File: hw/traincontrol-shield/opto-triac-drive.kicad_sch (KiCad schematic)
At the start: 6 parts, among them U5 MOC3021M, U6 MOC3021M

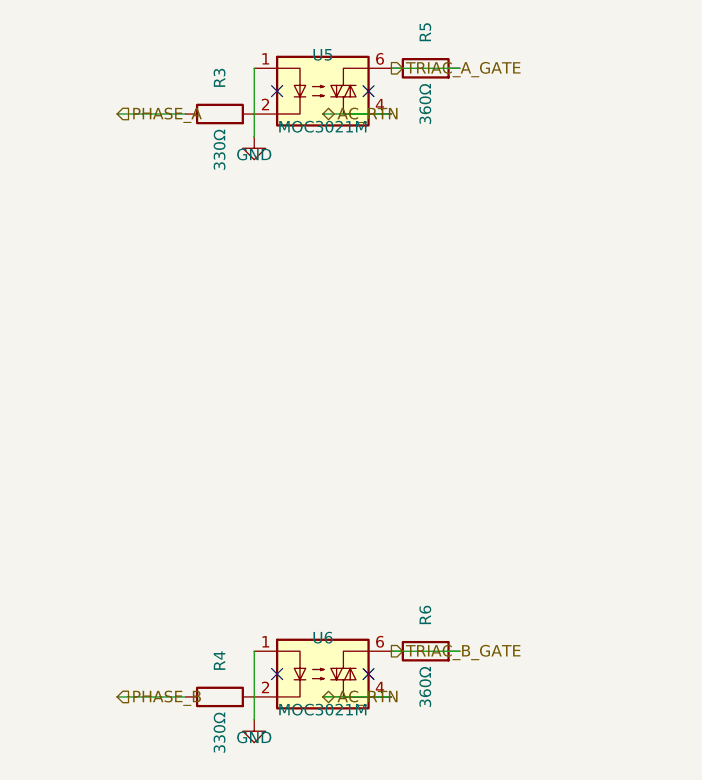
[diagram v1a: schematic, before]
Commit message: Fix hierarchical label placement and orientation in sub-sheets
Root cause: hlabel() placed the label at lx (stub tip) instead of x
(circuit connection point), mirroring the Issue-2 glabel bug fixed in
commit 2270223.

Fix applied to hlabel():
  (at {lx} ...) → (at {x} ...)  — label now sits at the circuit endpoint

Angle convention (matches label body direction):
  angle=180 → body extends LEFT  — left-side input/bidirectional labels
  angle=0   → body extends RIGHT — right-side output/bidirectional labels

Sheets affected: zero-crossing, xor-interlock, opto-triac-drive,
rail-voltage-sense; triacs-snubbers and mcu already had correct angles.

Co-Authored-By: Claude Sonnet 4.6 <noreply@anthropic.com>
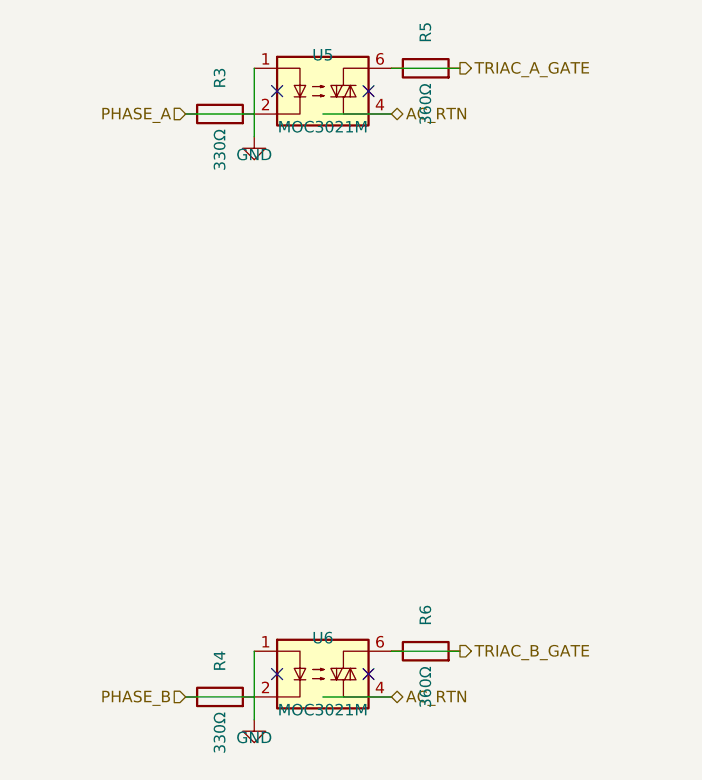
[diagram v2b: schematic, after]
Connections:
- net PHASE_A: now also R3.2, U5.2
- net PHASE_B: now also R4.2, U6.2
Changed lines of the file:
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@@
 	(hierarchical_label "AC_RTN"
 		(shape bidirectional)
-		(at 80.01 92.71000000000001 0)
+		(at 87.63000000000001 92.71000000000001 0)
 		(fields_autoplaced yes)
 		(effects (font (size 1.27 1.27)) (justify left bottom))
 		(property "Intersheetrefs" "${INTERSHEET_REFS}"
-			(at 80.01 92.71000000000001 0)
+			(at 87.63000000000001 92.71000000000001 0)
 			(effects (font (size 1.27 1.27)) (hide yes))
 		)
@@
 	)
 	(wire
-		(pts (xy 57.15 92.71000000000001) (xy 64.77 92.71000000000001))
+		(pts (xy 64.77 92.71000000000001) (xy 72.39 92.71000000000001))
 		(stroke (width 0) (type solid))
 	)
 	(hierarchical_label "PHASE_A"
 		(shape input)
-		(at 57.15 92.71000000000001 0)
-		(fields_autoplaced yes)
-		(effects (font (size 1.27 1.27)) (justify left bottom))
-		(property "Intersheetrefs" "${INTERSHEET_REFS}"
-			(at 57.15 92.71000000000001 0)
+		(at 64.77 92.71000000000001 180)
+		(fields_autoplaced yes)
+		(effects (font (size 1.27 1.27)) (justify right bottom))
+		(property "Intersheetrefs" "${INTERSHEET_REFS}"
+			(at 64.77 92.71000000000001 0)
 			(effects (font (size 1.27 1.27)) (hide yes))
 		)
@@
 	(hierarchical_label "TRIAC_A_GATE"
 		(shape output)
-		(at 87.63000000000001 87.63 0)
+		(at 95.25000000000001 87.63 0)
 		(fields_autoplaced yes)
 		(effects (font (size 1.27 1.27)) (justify left bottom))
 		(property "Intersheetrefs" "${INTERSHEET_REFS}"
-			(at 87.63000000000001 87.63 0)
+			(at 95.25000000000001 87.63 0)
 			(effects (font (size 1.27 1.27)) (hide yes))
 		)
@@
 	(hierarchical_label "AC_RTN"
 		(shape bidirectional)
-		(at 80.01 157.48 0)
+		(at 87.63000000000001 157.48 0)
 		(fields_autoplaced yes)
 		(effects (font (size 1.27 1.27)) (justify left bottom))
 		(property "Intersheetrefs" "${INTERSHEET_REFS}"
-			(at 80.01 157.48 0)
+			(at 87.63000000000001 157.48 0)
 			(effects (font (size 1.27 1.27)) (hide yes))
 		)
@@
 	)
 	(wire
-		(pts (xy 57.15 157.48) (xy 64.77 157.48))
+		(pts (xy 64.77 157.48) (xy 72.39 157.48))
 		(stroke (width 0) (type solid))
 	)
 	(hierarchical_label "PHASE_B"
 		(shape input)
-		(at 57.15 157.48 0)
-		(fields_autoplaced yes)
-		(effects (font (size 1.27 1.27)) (justify left bottom))
-		(property "Intersheetrefs" "${INTERSHEET_REFS}"
-			(at 57.15 157.48 0)
+		(at 64.77 157.48 180)
+		(fields_autoplaced yes)
+		(effects (font (size 1.27 1.27)) (justify right bottom))
+		(property "Intersheetrefs" "${INTERSHEET_REFS}"
+			(at 64.77 157.48 0)
 			(effects (font (size 1.27 1.27)) (hide yes))
 		)
@@
 	(hierarchical_label "TRIAC_B_GATE"
 		(shape output)
-		(at 87.63000000000001 152.4 0)
+		(at 95.25000000000001 152.4 0)
 		(fields_autoplaced yes)
 		(effects (font (size 1.27 1.27)) (justify left bottom))
 		(property "Intersheetrefs" "${INTERSHEET_REFS}"
-			(at 87.63000000000001 152.4 0)
-			(effects (font (size 1.27 1.27)) (hide yes))
-		)
+			(at 95.25000000000001 152.4 0)
+			(effects (font (size 1.27 1.27)) (hide yes))
+		)

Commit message: Fix stub wire short-circuit across R3/R5 in opto-triac sheet
With the label placed at x (circuit pin), the STUB wire from x to lx
was spanning the entire resistor body — creating a direct short across
both the LED series resistor (R3/R4) and the gate resistor (R5/R6).

Fix: shift x outward by one STUB so the stub wire terminates at the
resistor's outer pin rather than running across it:
  phase label:  x = cx-7.62-3.81-3.81-STUB  (lx lands on R pin2)
  gate  label:  x = gx+3.81+STUB             (lx lands on R gate pin1)

Co-Authored-By: Claude Sonnet 4.6 <noreply@anthropic.com>
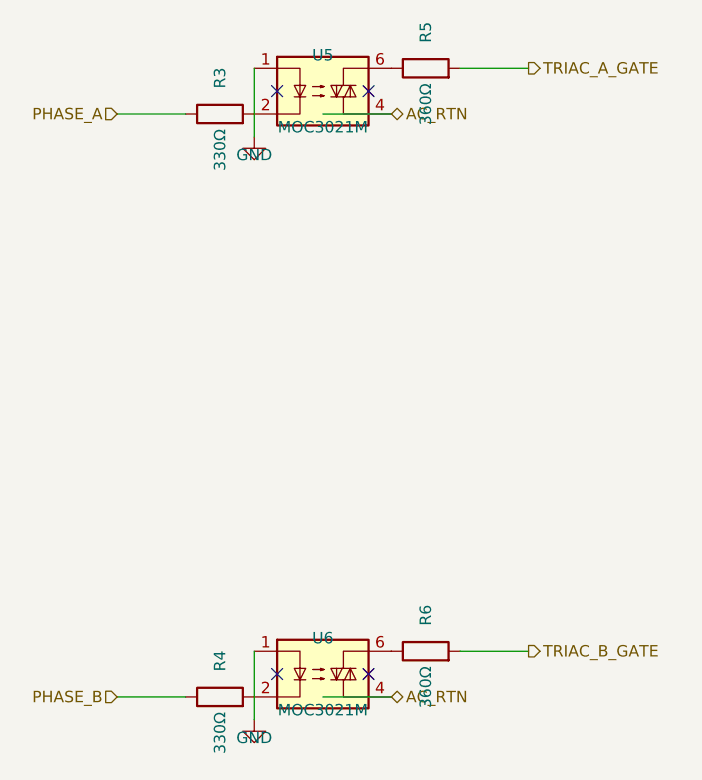
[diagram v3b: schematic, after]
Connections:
- net PHASE_A: no longer R3.2, U5.2
- net PHASE_B: no longer R4.2, U6.2
- net TRIAC_A_GATE: no longer R5.1, U5.6
- net TRIAC_B_GATE: no longer R6.1, U6.6
- new net: R4.2, U6.2
- new net: R6.1, U6.6
- new net: R3.2, U5.2
- new net: R5.1, U5.6
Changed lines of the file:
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@@
 	)
 	(wire
-		(pts (xy 64.77 92.71000000000001) (xy 72.39 92.71000000000001))
+		(pts (xy 57.15 92.71000000000001) (xy 64.77 92.71000000000001))
 		(stroke (width 0) (type solid))
 	)
 	(hierarchical_label "PHASE_A"
 		(shape input)
-		(at 64.77 92.71000000000001 180)
+		(at 57.15 92.71000000000001 180)
 		(fields_autoplaced yes)
 		(effects (font (size 1.27 1.27)) (justify right bottom))
 		(property "Intersheetrefs" "${INTERSHEET_REFS}"
-			(at 64.77 92.71000000000001 0)
+			(at 57.15 92.71000000000001 0)
 			(effects (font (size 1.27 1.27)) (hide yes))
 		)
@@
 	)
 	(wire
-		(pts (xy 87.63000000000001 87.63) (xy 95.25000000000001 87.63))
+		(pts (xy 95.25000000000001 87.63) (xy 102.87000000000002 87.63))
 		(stroke (width 0) (type solid))
 	)
 	(hierarchical_label "TRIAC_A_GATE"
 		(shape output)
-		(at 95.25000000000001 87.63 0)
+		(at 102.87000000000002 87.63 0)
 		(fields_autoplaced yes)
 		(effects (font (size 1.27 1.27)) (justify left bottom))
 		(property "Intersheetrefs" "${INTERSHEET_REFS}"
-			(at 95.25000000000001 87.63 0)
+			(at 102.87000000000002 87.63 0)
 			(effects (font (size 1.27 1.27)) (hide yes))
 		)
@@
 	)
 	(wire
-		(pts (xy 64.77 157.48) (xy 72.39 157.48))
+		(pts (xy 57.15 157.48) (xy 64.77 157.48))
 		(stroke (width 0) (type solid))
 	)
 	(hierarchical_label "PHASE_B"
 		(shape input)
-		(at 64.77 157.48 180)
+		(at 57.15 157.48 180)
 		(fields_autoplaced yes)
 		(effects (font (size 1.27 1.27)) (justify right bottom))
 		(property "Intersheetrefs" "${INTERSHEET_REFS}"
-			(at 64.77 157.48 0)
+			(at 57.15 157.48 0)
 			(effects (font (size 1.27 1.27)) (hide yes))
 		)
@@
 	)
 	(wire
-		(pts (xy 87.63000000000001 152.4) (xy 95.25000000000001 152.4))
+		(pts (xy 95.25000000000001 152.4) (xy 102.87000000000002 152.4))
 		(stroke (width 0) (type solid))
 	)
 	(hierarchical_label "TRIAC_B_GATE"
 		(shape output)
-		(at 95.25000000000001 152.4 0)
+		(at 102.87000000000002 152.4 0)
 		(fields_autoplaced yes)
 		(effects (font (size 1.27 1.27)) (justify left bottom))
 		(property "Intersheetrefs" "${INTERSHEET_REFS}"
-			(at 95.25000000000001 152.4 0)
-			(effects (font (size 1.27 1.27)) (hide yes))
-		)
+			(at 102.87000000000002 152.4 0)
+			(effects (font (size 1.27 1.27)) (hide yes))
+		)

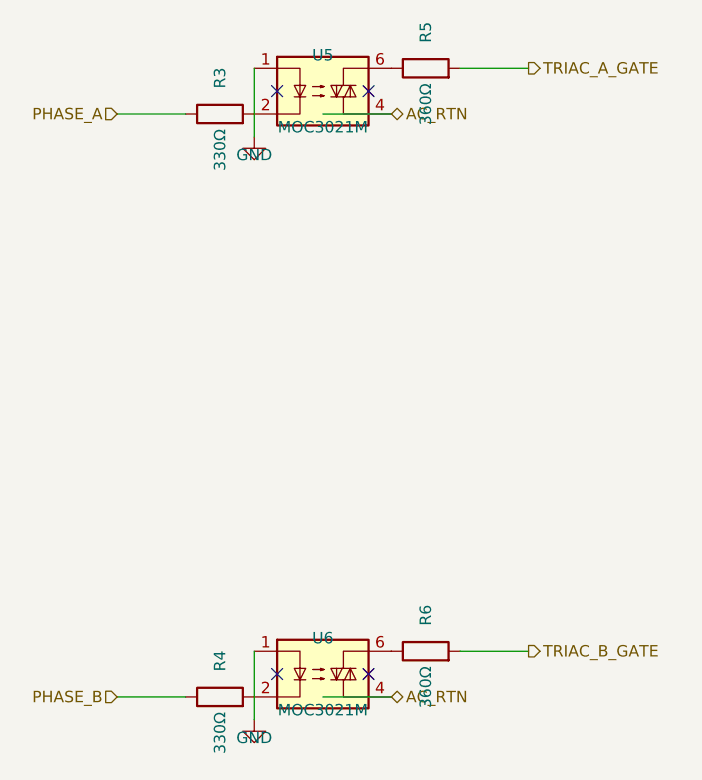
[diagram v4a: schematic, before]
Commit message: Fix hlabel stub direction: stubs now extend away from IC, not into it
Root cause: hlabel() used dx = +STUB for angle=180 and -STUB for angle=0,
which caused every stub wire to run INTO the IC body instead of outward.
This made wires appear to connect at the inner (wrong) end of all pins.

Fix: negate dx so stubs always extend outward from the pin tip:
  angle=180 (left-side input):  dx = -STUB → stub extends LEFT  ✓
  angle=0   (right-side output): dx = +STUB → stub extends RIGHT ✓

Also revert the x-position workarounds that compensated for the wrong
stub direction (zero-crossing AC_IN, opto-triac PHASE/GATE, power-supply
AC_IN/RTN): these are now back at the actual component pin positions.

All 8 sheets validate with kicad-cli.

Co-Authored-By: Claude Sonnet 4.6 <noreply@anthropic.com>
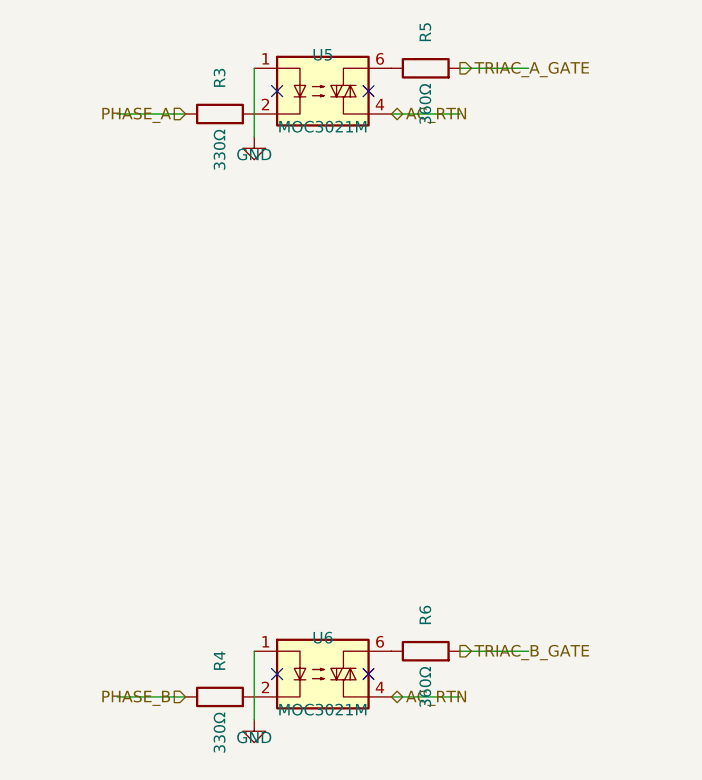
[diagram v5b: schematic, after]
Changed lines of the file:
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@@
 	)
 	(wire
-		(pts (xy 80.01 92.71000000000001) (xy 87.63000000000001 92.71000000000001))
+		(pts (xy 87.63000000000001 92.71000000000001) (xy 95.25000000000001 92.71000000000001))
 		(stroke (width 0) (type solid))
 	)
@@
 	(hierarchical_label "PHASE_A"
 		(shape input)
-		(at 57.15 92.71000000000001 180)
+		(at 64.77 92.71000000000001 180)
 		(fields_autoplaced yes)
 		(effects (font (size 1.27 1.27)) (justify right bottom))
 		(property "Intersheetrefs" "${INTERSHEET_REFS}"
-			(at 57.15 92.71000000000001 0)
+			(at 64.77 92.71000000000001 0)
 			(effects (font (size 1.27 1.27)) (hide yes))
 		)
@@
 	(hierarchical_label "TRIAC_A_GATE"
 		(shape output)
-		(at 102.87000000000002 87.63 0)
+		(at 95.25000000000001 87.63 0)
 		(fields_autoplaced yes)
 		(effects (font (size 1.27 1.27)) (justify left bottom))
 		(property "Intersheetrefs" "${INTERSHEET_REFS}"
-			(at 102.87000000000002 87.63 0)
+			(at 95.25000000000001 87.63 0)
 			(effects (font (size 1.27 1.27)) (hide yes))
 		)
@@
 	)
 	(wire
-		(pts (xy 80.01 157.48) (xy 87.63000000000001 157.48))
+		(pts (xy 87.63000000000001 157.48) (xy 95.25000000000001 157.48))
 		(stroke (width 0) (type solid))
 	)
@@
 	(hierarchical_label "PHASE_B"
 		(shape input)
-		(at 57.15 157.48 180)
+		(at 64.77 157.48 180)
 		(fields_autoplaced yes)
 		(effects (font (size 1.27 1.27)) (justify right bottom))
 		(property "Intersheetrefs" "${INTERSHEET_REFS}"
-			(at 57.15 157.48 0)
+			(at 64.77 157.48 0)
 			(effects (font (size 1.27 1.27)) (hide yes))
 		)
@@
 	(hierarchical_label "TRIAC_B_GATE"
 		(shape output)
-		(at 102.87000000000002 152.4 0)
+		(at 95.25000000000001 152.4 0)
 		(fields_autoplaced yes)
 		(effects (font (size 1.27 1.27)) (justify left bottom))
 		(property "Intersheetrefs" "${INTERSHEET_REFS}"
-			(at 102.87000000000002 152.4 0)
-			(effects (font (size 1.27 1.27)) (hide yes))
-		)
+			(at 95.25000000000001 152.4 0)
+			(effects (font (size 1.27 1.27)) (hide yes))
+		)

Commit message: Fix hlabel placement: label sits at stub outer end (lx), not pin tip (x)
The hierarchical label connection point must be at lx (the outer end of
the stub wire), not at x (the IC pin tip). With the label at x, it was
overlapping the pin itself instead of sitting at the end of the routing
stub where it belongs.

  angle=180 (left-side): lx = x - STUB  → label to the left of pin ✓
  angle=0   (right-side): lx = x + STUB  → label to the right of pin ✓

Wire still runs x↔lx, connecting the IC pin to the label connection.
Updated gen_all_sheets.py and gen_power_supply.py.

Co-Authored-By: Claude Sonnet 4.6 <noreply@anthropic.com>
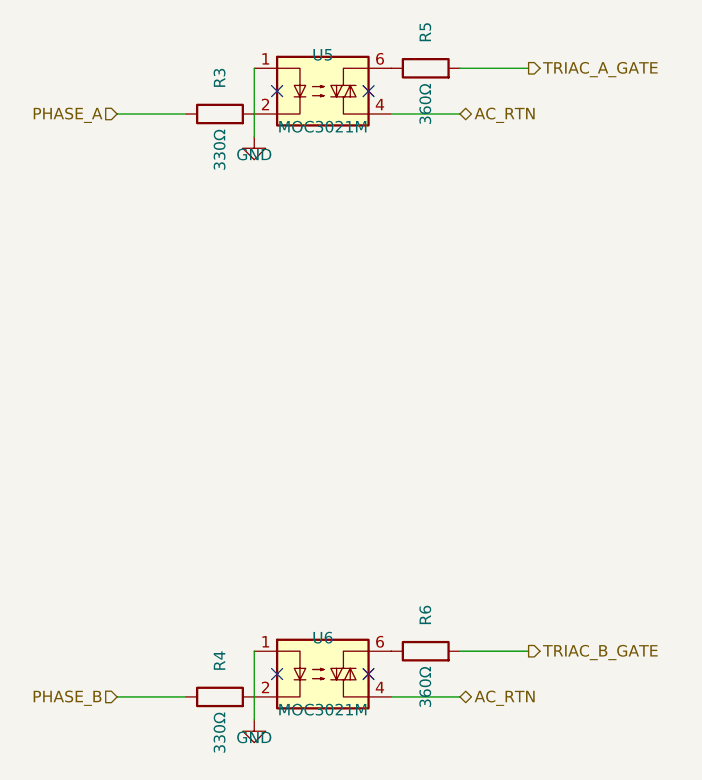
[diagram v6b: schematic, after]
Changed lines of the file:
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@@
 	(hierarchical_label "AC_RTN"
 		(shape bidirectional)
-		(at 87.63000000000001 92.71000000000001 0)
+		(at 95.25000000000001 92.71000000000001 0)
 		(fields_autoplaced yes)
 		(effects (font (size 1.27 1.27)) (justify left bottom))
 		(property "Intersheetrefs" "${INTERSHEET_REFS}"
-			(at 87.63000000000001 92.71000000000001 0)
+			(at 95.25000000000001 92.71000000000001 0)
 			(effects (font (size 1.27 1.27)) (hide yes))
 		)
@@
 	(hierarchical_label "PHASE_A"
 		(shape input)
-		(at 64.77 92.71000000000001 180)
+		(at 57.15 92.71000000000001 180)
 		(fields_autoplaced yes)
 		(effects (font (size 1.27 1.27)) (justify right bottom))
 		(property "Intersheetrefs" "${INTERSHEET_REFS}"
-			(at 64.77 92.71000000000001 0)
+			(at 57.15 92.71000000000001 0)
 			(effects (font (size 1.27 1.27)) (hide yes))
 		)
@@
 	(hierarchical_label "TRIAC_A_GATE"
 		(shape output)
-		(at 95.25000000000001 87.63 0)
+		(at 102.87000000000002 87.63 0)
 		(fields_autoplaced yes)
 		(effects (font (size 1.27 1.27)) (justify left bottom))
 		(property "Intersheetrefs" "${INTERSHEET_REFS}"
-			(at 95.25000000000001 87.63 0)
+			(at 102.87000000000002 87.63 0)
 			(effects (font (size 1.27 1.27)) (hide yes))
 		)
@@
 	(hierarchical_label "AC_RTN"
 		(shape bidirectional)
-		(at 87.63000000000001 157.48 0)
+		(at 95.25000000000001 157.48 0)
 		(fields_autoplaced yes)
 		(effects (font (size 1.27 1.27)) (justify left bottom))
 		(property "Intersheetrefs" "${INTERSHEET_REFS}"
-			(at 87.63000000000001 157.48 0)
+			(at 95.25000000000001 157.48 0)
 			(effects (font (size 1.27 1.27)) (hide yes))
 		)
@@
 	(hierarchical_label "PHASE_B"
 		(shape input)
-		(at 64.77 157.48 180)
+		(at 57.15 157.48 180)
 		(fields_autoplaced yes)
 		(effects (font (size 1.27 1.27)) (justify right bottom))
 		(property "Intersheetrefs" "${INTERSHEET_REFS}"
-			(at 64.77 157.48 0)
+			(at 57.15 157.48 0)
 			(effects (font (size 1.27 1.27)) (hide yes))
 		)
@@
 	(hierarchical_label "TRIAC_B_GATE"
 		(shape output)
-		(at 95.25000000000001 152.4 0)
+		(at 102.87000000000002 152.4 0)
 		(fields_autoplaced yes)
 		(effects (font (size 1.27 1.27)) (justify left bottom))
 		(property "Intersheetrefs" "${INTERSHEET_REFS}"
-			(at 95.25000000000001 152.4 0)
-			(effects (font (size 1.27 1.27)) (hide yes))
-		)
+			(at 102.87000000000002 152.4 0)
+			(effects (font (size 1.27 1.27)) (hide yes))
+		)
